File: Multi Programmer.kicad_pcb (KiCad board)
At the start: 2 copper layers, 99.1 x 96.5 mm, 64 parts, among them J1 USB_B, J2 Serial, SW1 RESET, SW2 MODE, U1 TTLSW, U2 FT232RL, U3 ATmega328P-PU, U4 NE555, Y1 16MHz, Y2 16MHz

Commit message: Added sockets for attiny, move sockets to separate page
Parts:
- removed JP1, JP2: Jumper, Connector_PinHeader_2.54mm:PinHeader_1x02_P2.54mm_Vertical
- added C24: 100n, Capacitor_SMD:C_0805_2012Metric_Pad1.15x1.40mm_HandSolder, B.Cu at (167.6, 77.2)
- added C25: 100n, Capacitor_SMD:C_0805_2012Metric_Pad1.15x1.40mm_HandSolder, B.Cu at (167.6, 64.8)
- added SK3: ATtiny45/85, Package_DIP:DIP-8_W7.62mm, F.Cu at (167.6, 81.3)
- added SK4: ATtiny44/84, Package_DIP:DIP-14_W7.62mm, F.Cu at (167.6, 68.6)
- moved C11 50.8 mm to (133.3, 79.4), turned to 90 degrees
- moved C12 48.3 mm to (133.3, 72.4), turned to 270 degrees
- moved Y2 43.0 mm to (137.2, 78.7), turned to 90 degrees
- moved R4 36.3 mm to (185.4, 111.8)
- moved D11 27.8 mm to (181.6, 110.5), turned to 90 degrees
- moved C7 18.1 mm to (185.4, 106.7)
- moved C10 11.4 mm to (174.0, 125.7)
- moved C5 11.4 mm to (174.0, 90.2)
- moved U1 11.4 mm to (170.2, 88.9)
- moved C17 11.4 mm to (174.0, 118.1)
- moved U4 11.4 mm to (170.2, 118.1)
- moved R5 8.03 mm to (174.0, 123.2), turned to 0 degrees
- moved R6 3.81 mm to (174.0, 120.7), turned to 0 degrees
- moved F1 3.42 mm to (182.9, 119.4), turned to 270 degrees
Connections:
- C11 pad 2: Net-(C11-Pad2) -> /Sockets/S_XTAL1
- C12 pad 2: Net-(C12-Pad2) -> /Sockets/S_XTAL2
- SK1 pad 15: /S_MOSI -> /Sockets/S_MOSI
- SK1 pad 16: /S_MISO -> /Sockets/S_MISO
- SK1 pad 17: /S_SCK -> /Sockets/S_SCK
- SK1 pad 29: /~SCK_RST -> /Sockets/~SCK_RST
- SK1 pad 30: /TXD_SER -> /Sockets/TXD_SER
- SK1 pad 31: /RXD_SER -> /Sockets/RXD_SER
- SK1 pad 7: /S_XTAL1 -> /Sockets/S_XTAL1
- SK1 pad 8: /S_XTAL2 -> /Sockets/S_XTAL2
- SK2 pad 1: /~SCK_RST -> /Sockets/~SCK_RST
- SK2 pad 10: /S_XTAL2 -> /Sockets/S_XTAL2
- SK2 pad 17: /S_MOSI -> /Sockets/S_MOSI
- SK2 pad 18: /S_MISO -> /Sockets/S_MISO
- SK2 pad 19: /S_SCK -> /Sockets/S_SCK
- SK2 pad 2: /TXD_SER -> /Sockets/TXD_SER
- SK2 pad 3: /RXD_SER -> /Sockets/RXD_SER
- SK2 pad 9: /S_XTAL1 -> /Sockets/S_XTAL1
- Y2 pad 1: Net-(C11-Pad2) -> /Sockets/S_XTAL1
- Y2 pad 2: Net-(C12-Pad2) -> /Sockets/S_XTAL2
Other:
- board text added: "ATMEGA328P DIP 28 PINS"
- board text added: "ATMEGA328P TQFP 32 PINS"
- board text added: "ATTINY44/84"
- board text added: "ATTINY45/85"
- board text added: "Multi Programmer / Rev A / 2019 Dominic Thibodeau / dev@hotkeysoft.net"
- board text removed: "ATMEGA328P-AU TQFP 32 PINS"
- board text removed: "ATMEGA328P-PU DIP 28 PINS"
- board text removed: "Multi Programmer Rev A 2019 Dominic Thibodeau dev@hotkeysoft.net"
- board text removed: "SOCKET CLOCK"

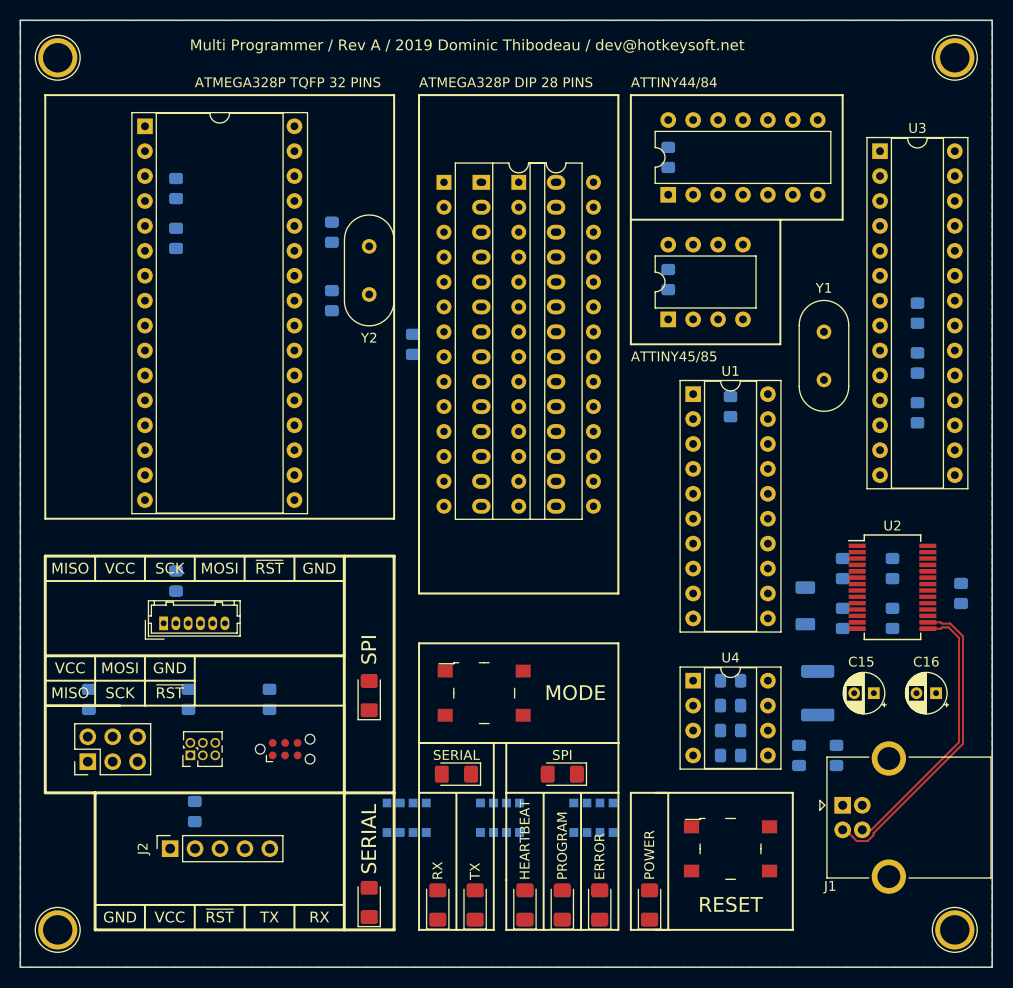
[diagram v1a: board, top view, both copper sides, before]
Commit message: 
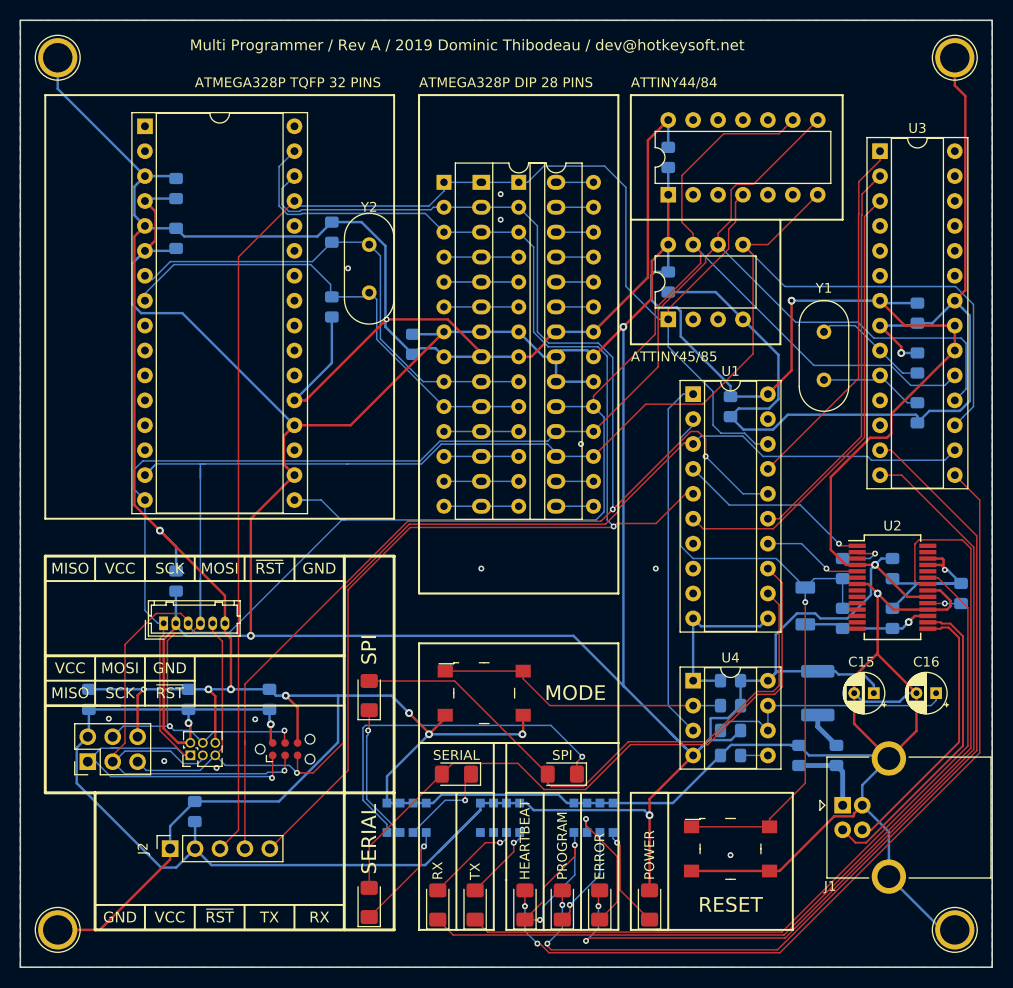
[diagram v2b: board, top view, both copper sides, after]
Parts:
- C11, C12: value 22p -> 100n
- C24, C25, C8, C9: value 100n -> 22
- moved C25 37.5 mm to (133.3, 80.0), turned to 90 degrees
- moved C12 35.1 mm to (167.6, 64.8)
- moved C24 34.6 mm to (133.3, 72.4), turned to 270 degrees
- moved C11 34.3 mm to (167.6, 77.5)
- moved Y2 5.08 mm to (137.2, 73.7), turned to 270 degrees
- turned F1 to 90 degrees
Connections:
- C11 pad 2: /Sockets/S_XTAL1 -> VCC
- C12 pad 2: /Sockets/S_XTAL2 -> VCC
- C24 pad 2: VCC -> /S_XTAL1
- C25 pad 2: VCC -> /S_XTAL2
- F1 pad 1: VCC -> /VFUSE
- F1 pad 2: /VFUSE -> VCC
- SK1 pad 15: /Sockets/S_MOSI -> /S_MOSI
- SK1 pad 16: /Sockets/S_MISO -> /S_MISO
- SK1 pad 17: /Sockets/S_SCK -> /S_SCK
- SK1 pad 29: /Sockets/~SCK_RST -> /~SCK_RST
- SK1 pad 30: /Sockets/TXD_SER -> /TXD_SER
- SK1 pad 31: /Sockets/RXD_SER -> /RXD_SER
- SK1 pad 7: /Sockets/S_XTAL1 -> /S_XTAL1
- SK1 pad 8: /Sockets/S_XTAL2 -> /S_XTAL2
- SK2 pad 1: /Sockets/~SCK_RST -> /~SCK_RST
- SK2 pad 10: /Sockets/S_XTAL2 -> /S_XTAL2
- SK2 pad 17: /Sockets/S_MOSI -> /S_MOSI
- SK2 pad 18: /Sockets/S_MISO -> /S_MISO
- SK2 pad 19: /Sockets/S_SCK -> /S_SCK
- SK2 pad 2: /Sockets/TXD_SER -> /TXD_SER
- SK2 pad 3: /Sockets/RXD_SER -> /RXD_SER
- SK2 pad 9: /Sockets/S_XTAL1 -> /S_XTAL1
- SK3 pad 1: /Sockets/~SCK_RST -> /~SCK_RST
- SK3 pad 5: /Sockets/S_MOSI -> /S_MOSI
- SK3 pad 6: /Sockets/S_MISO -> /S_MISO
- SK3 pad 7: /Sockets/S_SCK -> /S_SCK
- SK4 pad 4: /Sockets/~SCK_RST -> /~SCK_RST
- SK4 pad 7: /Sockets/S_MOSI -> /S_MOSI
- SK4 pad 8: /Sockets/S_MISO -> /S_MISO
- SK4 pad 9: /Sockets/S_SCK -> /S_SCK
- Y2 pad 1: /Sockets/S_XTAL1 -> /S_XTAL1
- Y2 pad 2: /Sockets/S_XTAL2 -> /S_XTAL2
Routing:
- net GND: track 0.00 -> 615.1 mm, vias 0 -> 23
- net VCC: track 0.00 -> 526.7 mm, vias 0 -> 7
- net /S_SCK: track 0.00 -> 197.1 mm, vias 0 -> 1
- net /S_MISO: track 0.00 -> 192.9 mm, vias 0 -> 1
- net /S_MOSI: track 0.00 -> 186.1 mm, vias 0 -> 2
- net /~SCK_RST: track 0.00 -> 157.0 mm
- net /TXD_SER: track 0.00 -> 150.5 mm, vias 0 -> 2
- net /RXD_SER: track 0.00 -> 137.7 mm, vias 0 -> 1
- net /~RST_ICSP: track 0.00 -> 125.9 mm, vias 0 -> 1
- net /~RX_LED: track 0.00 -> 94.7 mm
- net /PRG_LED: track 0.00 -> 94.0 mm, vias 0 -> 2
- net /HB_LED: track 0.00 -> 89.2 mm, vias 0 -> 2
- net /ERR_LED: track 0.00 -> 86.6 mm, vias 0 -> 2
- net /~TX_LED: track 0.00 -> 78.1 mm
- net /~RESET: track 0.00 -> 69.0 mm, vias 0 -> 1
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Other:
- net class VBUS: via_dia 0.6 -> 0.8; via_drill 0.3 -> 0.4
